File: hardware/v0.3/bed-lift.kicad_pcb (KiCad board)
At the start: 4 copper layers, 175 x 40 mm, 117 parts, among them J1 SM04B-SRSS-TB, J10 S4B-XH-A, J11 S4B-XH-A, J12 S4B-XH-A, J13 S4B-XH-A, J2 S2P-VH, J3 SM04B-SRSS-TB, J4 TC2030-NL, J5 PH1-06-UA, J6 S3B-XH-A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

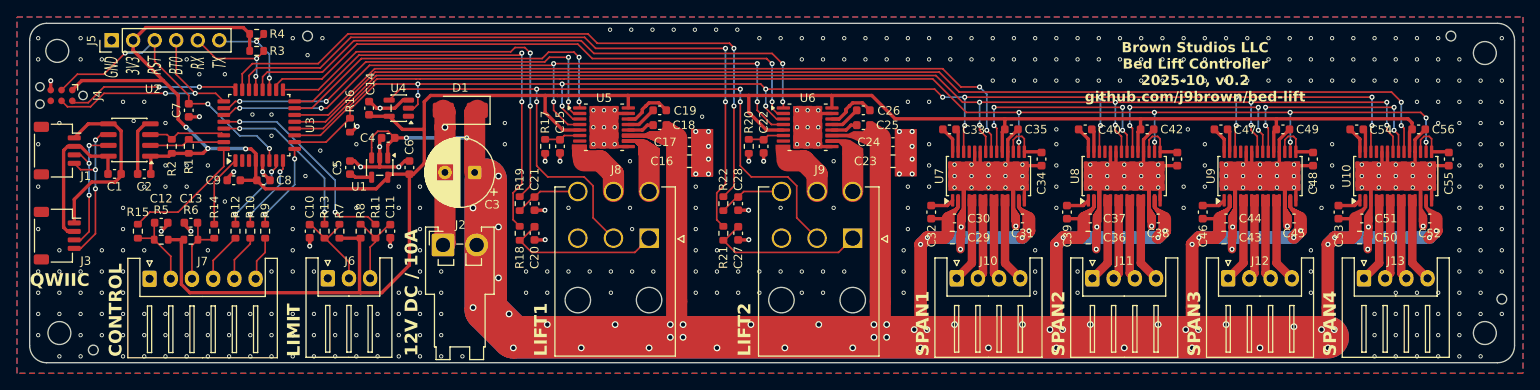
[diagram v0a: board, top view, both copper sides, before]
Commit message: Update v0.3 to address errata.
Moved the board design and errata into a versioned documents.
Added some photos of the bed.
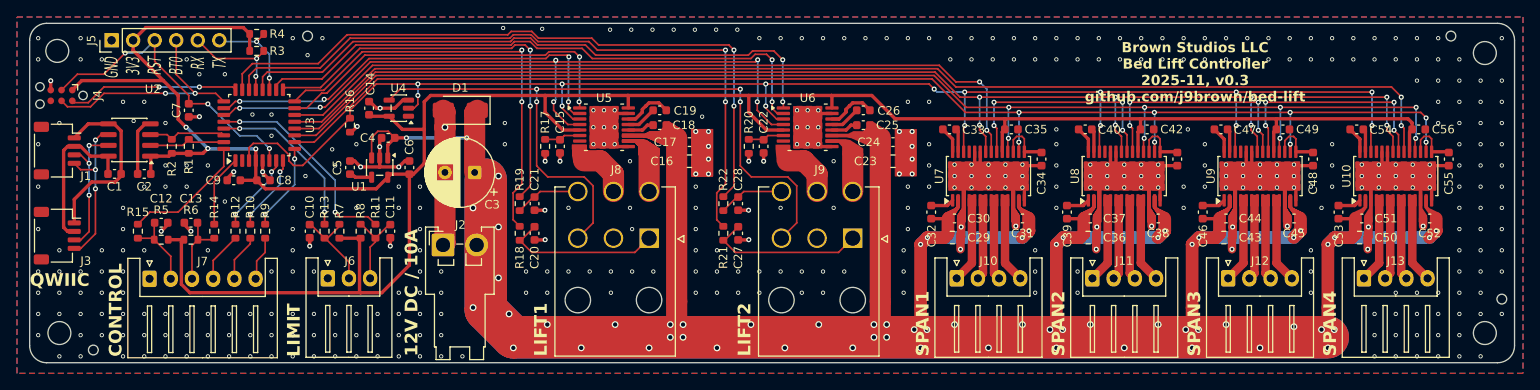
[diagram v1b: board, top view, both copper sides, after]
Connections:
- J8 pad 2: /VHALL -> GND
- J8 pad 3: GND -> /VHALL
- J9 pad 2: /VHALL -> GND
- J9 pad 3: GND -> /VHALL
- U10 pad 18: GND -> /SPI1_NSS
- U3 pad 10: /~{DRV_SLEEP} -> /~{SPAN_FAULT}
- U3 pad 11: /~{SPAN_FAULT} -> /SPI1_NSS
- U3 pad 3: unconnected-(U3-PC15-Pad3) -> /~{DRV_SLEEP}
- U7 pad 18: GND -> /SPI1_NSS
- U8 pad 18: GND -> /SPI1_NSS
- U9 pad 18: GND -> /SPI1_NSS
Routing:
- net /SPI1_NSS: track 0.00 -> 157.8 mm, vias 0 -> 8
- net GND: track 123.2 -> 105.3 mm, vias 477 -> 451
- net /~{DRV_SLEEP}: track 171.1 -> 183.6 mm
- net /SPI1_SCLK: track 157.2 -> 159.7 mm
- net /~{LIFT_FAULT}: track 83.5 -> 84.8 mm
- net /span1/SDO: track 26.0 -> 27.3 mm
- net /span3/SDO: track 25.8 -> 27.0 mm
- net /span2/SDO: track 26.0 -> 27.2 mm
- net /LIFT2_IN1: track 71.1 -> 72.1 mm
- net /LIFT2_IN2: track 68.4 -> 69.4 mm
- net /SPI1_SDO: track 92.1 -> 92.8 mm
- net /SPI1_SDI: track 140.3 -> 141.0 mm
